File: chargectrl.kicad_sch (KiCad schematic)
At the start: 84 parts, among them Q2 SiRA00DP, Q3 SiRA00DP, Q4 SiRA00DP, Q5 SiRA00DP, U4 BQ25756RRVR, U5 TPS25730D, U6 MAX17614ATP+, U7 MAX17614ATP+

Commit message: Finalized V2
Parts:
- removed TP19, TP22: TEST POINT, symbol Connector:TestPoint
- C50, C51, C52, C53, C54, C55, C56, C57, C58, C59, C60, C61, C62, C63, C64, C65, C66, C67, C68, C69, C70, C71, C72, C73, C74, C75, C76, C77, C78, C79: footprint Capacitor_SMD:C_0402_1005Metric -> Capacitor_SMD:C_0402_1005Metric_Pad0.74x0.62mm_HandSolder
- D10, D11: footprint Diode_SMD:D_0402_1005Metric -> Diode_SMD:D_0402_1005Metric_Pad0.77x0.64mm_HandSolder
- R51: renamed from R49; footprint Resistor_SMD:R_0402_1005Metric -> Resistor_SMD:R_0402_1005Metric_Pad0.72x0.64mm_HandSolder
- R52: renamed from R50; footprint Resistor_SMD:R_0402_1005Metric -> Resistor_SMD:R_0402_1005Metric_Pad0.72x0.64mm_HandSolder
- R53: renamed from R51; footprint Resistor_SMD:R_0402_1005Metric -> Resistor_SMD:R_0402_1005Metric_Pad0.72x0.64mm_HandSolder
- R54: renamed from R52; footprint Resistor_SMD:R_0402_1005Metric -> Resistor_SMD:R_0402_1005Metric_Pad0.72x0.64mm_HandSolder
- R55: renamed from R53; footprint Resistor_SMD:R_0402_1005Metric -> Resistor_SMD:R_0402_1005Metric_Pad0.72x0.64mm_HandSolder
- R56: renamed from R54; footprint Resistor_SMD:R_0402_1005Metric -> Resistor_SMD:R_0402_1005Metric_Pad0.72x0.64mm_HandSolder
- R57: renamed from R55; footprint Resistor_SMD:R_0402_1005Metric -> Resistor_SMD:R_0402_1005Metric_Pad0.72x0.64mm_HandSolder
- R58: renamed from R56; footprint Resistor_SMD:R_0402_1005Metric -> Resistor_SMD:R_0402_1005Metric_Pad0.72x0.64mm_HandSolder
- R59: renamed from R57; footprint Resistor_SMD:R_0402_1005Metric -> Resistor_SMD:R_0402_1005Metric_Pad0.72x0.64mm_HandSolder
- R60: renamed from R58; footprint Resistor_SMD:R_0402_1005Metric -> Resistor_SMD:R_0402_1005Metric_Pad0.72x0.64mm_HandSolder
- R61: renamed from R59; footprint Resistor_SMD:R_0402_1005Metric -> Resistor_SMD:R_0402_1005Metric_Pad0.72x0.64mm_HandSolder
- R62: renamed from R60; footprint Resistor_SMD:R_0402_1005Metric -> Resistor_SMD:R_0402_1005Metric_Pad0.72x0.64mm_HandSolder
- R63: renamed from R61; footprint Resistor_SMD:R_0402_1005Metric -> Resistor_SMD:R_0402_1005Metric_Pad0.72x0.64mm_HandSolder
- R64: renamed from R62; footprint Resistor_SMD:R_0402_1005Metric -> Resistor_SMD:R_0402_1005Metric_Pad0.72x0.64mm_HandSolder
- R65: renamed from R63; footprint Resistor_SMD:R_0402_1005Metric -> Resistor_SMD:R_0402_1005Metric_Pad0.72x0.64mm_HandSolder
- R66: renamed from R64; footprint Resistor_SMD:R_0402_1005Metric -> Resistor_SMD:R_0402_1005Metric_Pad0.72x0.64mm_HandSolder
- R67: renamed from R65; footprint Resistor_SMD:R_0402_1005Metric -> Resistor_SMD:R_0402_1005Metric_Pad0.72x0.64mm_HandSolder
- R68: renamed from R66; footprint Resistor_SMD:R_0402_1005Metric -> Resistor_SMD:R_0402_1005Metric_Pad0.72x0.64mm_HandSolder
- R69: renamed from R67; footprint Resistor_SMD:R_0402_1005Metric -> Resistor_SMD:R_0402_1005Metric_Pad0.72x0.64mm_HandSolder
- R70: renamed from R68; footprint Resistor_SMD:R_0402_1005Metric -> Resistor_SMD:R_0402_1005Metric_Pad0.72x0.64mm_HandSolder
- R71: renamed from R69; footprint Resistor_SMD:R_0402_1005Metric -> Resistor_SMD:R_0402_1005Metric_Pad0.72x0.64mm_HandSolder
- R72: renamed from R70; footprint Resistor_SMD:R_0402_1005Metric -> Resistor_SMD:R_0402_1005Metric_Pad0.72x0.64mm_HandSolder
- R73: renamed from R71; footprint Resistor_SMD:R_0402_1005Metric -> Resistor_SMD:R_0402_1005Metric_Pad0.72x0.64mm_HandSolder
- R74: renamed from R72; footprint Resistor_SMD:R_0402_1005Metric -> Resistor_SMD:R_0402_1005Metric_Pad0.72x0.64mm_HandSolder
- R75: renamed from R73; footprint Resistor_SMD:R_0402_1005Metric -> Resistor_SMD:R_0402_1005Metric_Pad0.72x0.64mm_HandSolder
- R76: renamed from R74; footprint Resistor_SMD:R_0402_1005Metric -> Resistor_SMD:R_0402_1005Metric_Pad0.72x0.64mm_HandSolder
- R77: renamed from R75; footprint Resistor_SMD:R_0402_1005Metric -> Resistor_SMD:R_0402_1005Metric_Pad0.72x0.64mm_HandSolder
- R78: renamed from R76; footprint Resistor_SMD:R_0402_1005Metric -> Resistor_SMD:R_0402_1005Metric_Pad0.72x0.64mm_HandSolder
- R79: renamed from R77; footprint Resistor_SMD:R_0402_1005Metric -> Resistor_SMD:R_0402_1005Metric_Pad0.72x0.64mm_HandSolder
- R80: renamed from R78; footprint Resistor_SMD:R_0402_1005Metric -> Resistor_SMD:R_0402_1005Metric_Pad0.72x0.64mm_HandSolder
- R81: renamed from R79; footprint Resistor_SMD:R_0402_1005Metric -> Resistor_SMD:R_0402_1005Metric_Pad0.72x0.64mm_HandSolder
- R82: renamed from R80; footprint Resistor_SMD:R_0402_1005Metric -> Resistor_SMD:R_0402_1005Metric_Pad0.72x0.64mm_HandSolder
- R83: renamed from R81; footprint Resistor_SMD:R_0402_1005Metric -> Resistor_SMD:R_0402_1005Metric_Pad0.72x0.64mm_HandSolder
- R84: renamed from R82; footprint Resistor_SMD:R_0402_1005Metric -> Resistor_SMD:R_0402_1005Metric_Pad0.72x0.64mm_HandSolder
- R85: renamed from R83; footprint Resistor_SMD:R_0402_1005Metric -> Resistor_SMD:R_0402_1005Metric_Pad0.72x0.64mm_HandSolder
- R86: renamed from R84; footprint Resistor_SMD:R_0402_1005Metric -> Resistor_SMD:R_0402_1005Metric_Pad0.72x0.64mm_HandSolder
- R87: renamed from R85; footprint Resistor_SMD:R_0402_1005Metric -> Resistor_SMD:R_0402_1005Metric_Pad0.72x0.64mm_HandSolder
- R88: renamed from R86; footprint Resistor_SMD:R_0402_1005Metric -> Resistor_SMD:R_0402_1005Metric_Pad0.72x0.64mm_HandSolder
- R89: renamed from R87; footprint Resistor_SMD:R_0402_1005Metric -> Resistor_SMD:R_0402_1005Metric_Pad0.72x0.64mm_HandSolder
- TP19: renamed from TP20; footprint (none) -> TestPoint:TestPoint_Pad_1.0x1.0mm
- TP20: renamed from TP21; footprint (none) -> TestPoint:TestPoint_Pad_1.0x1.0mm
- renumbered U4 to U6, U5 to U7, U6 to U8, U7 to U9

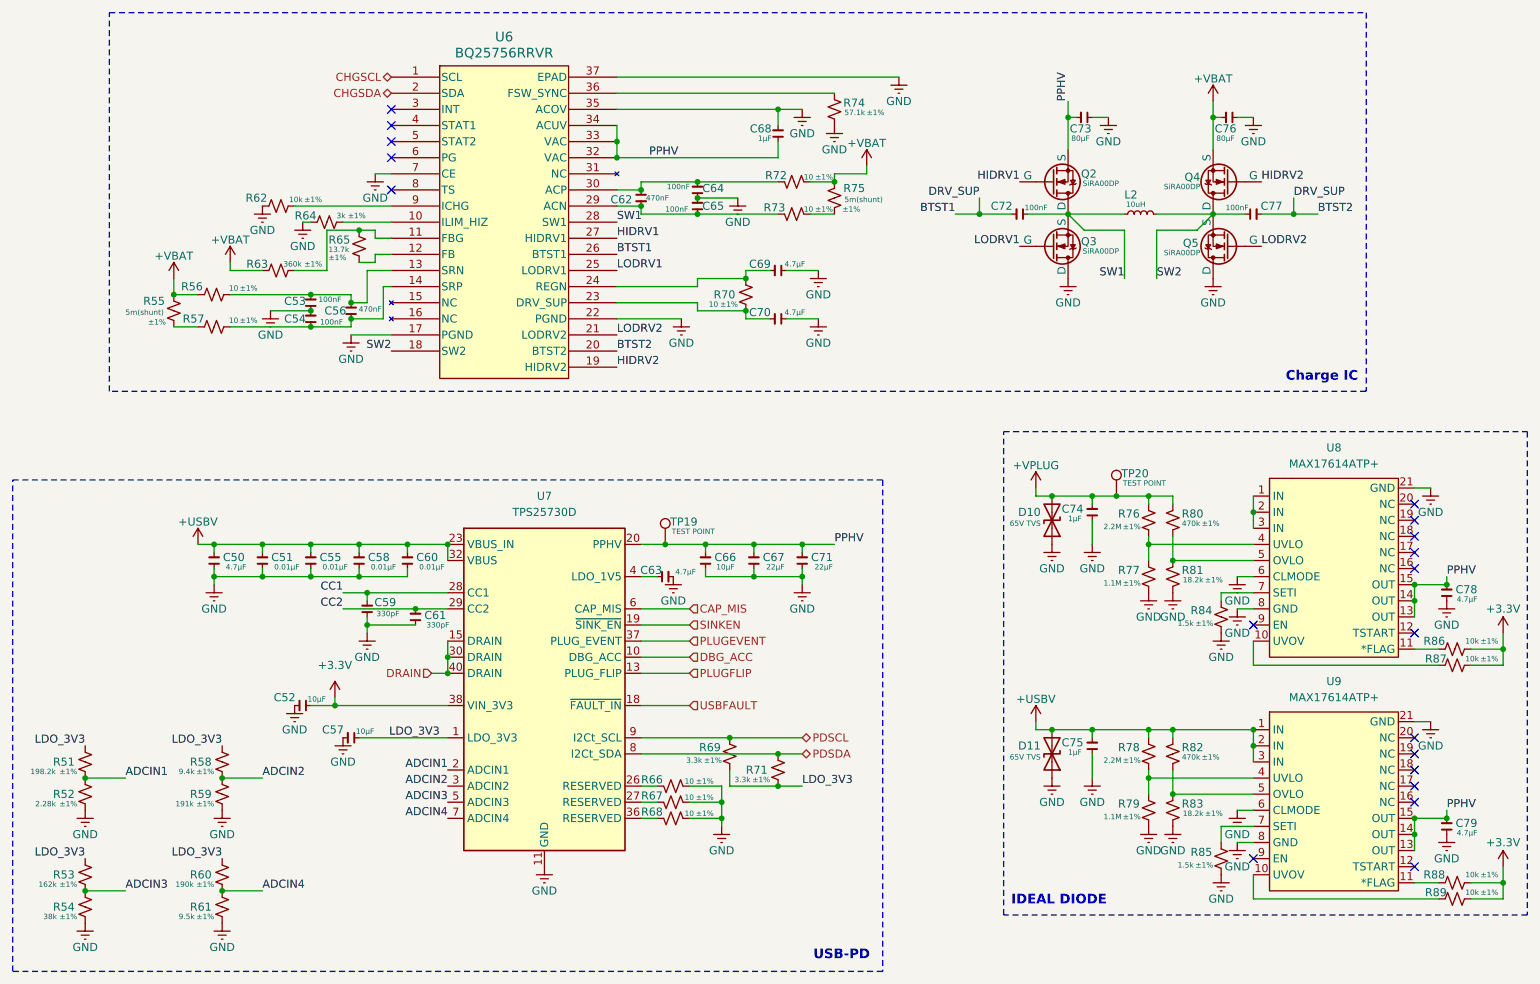
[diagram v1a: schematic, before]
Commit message: Fixed Ideal Diodes
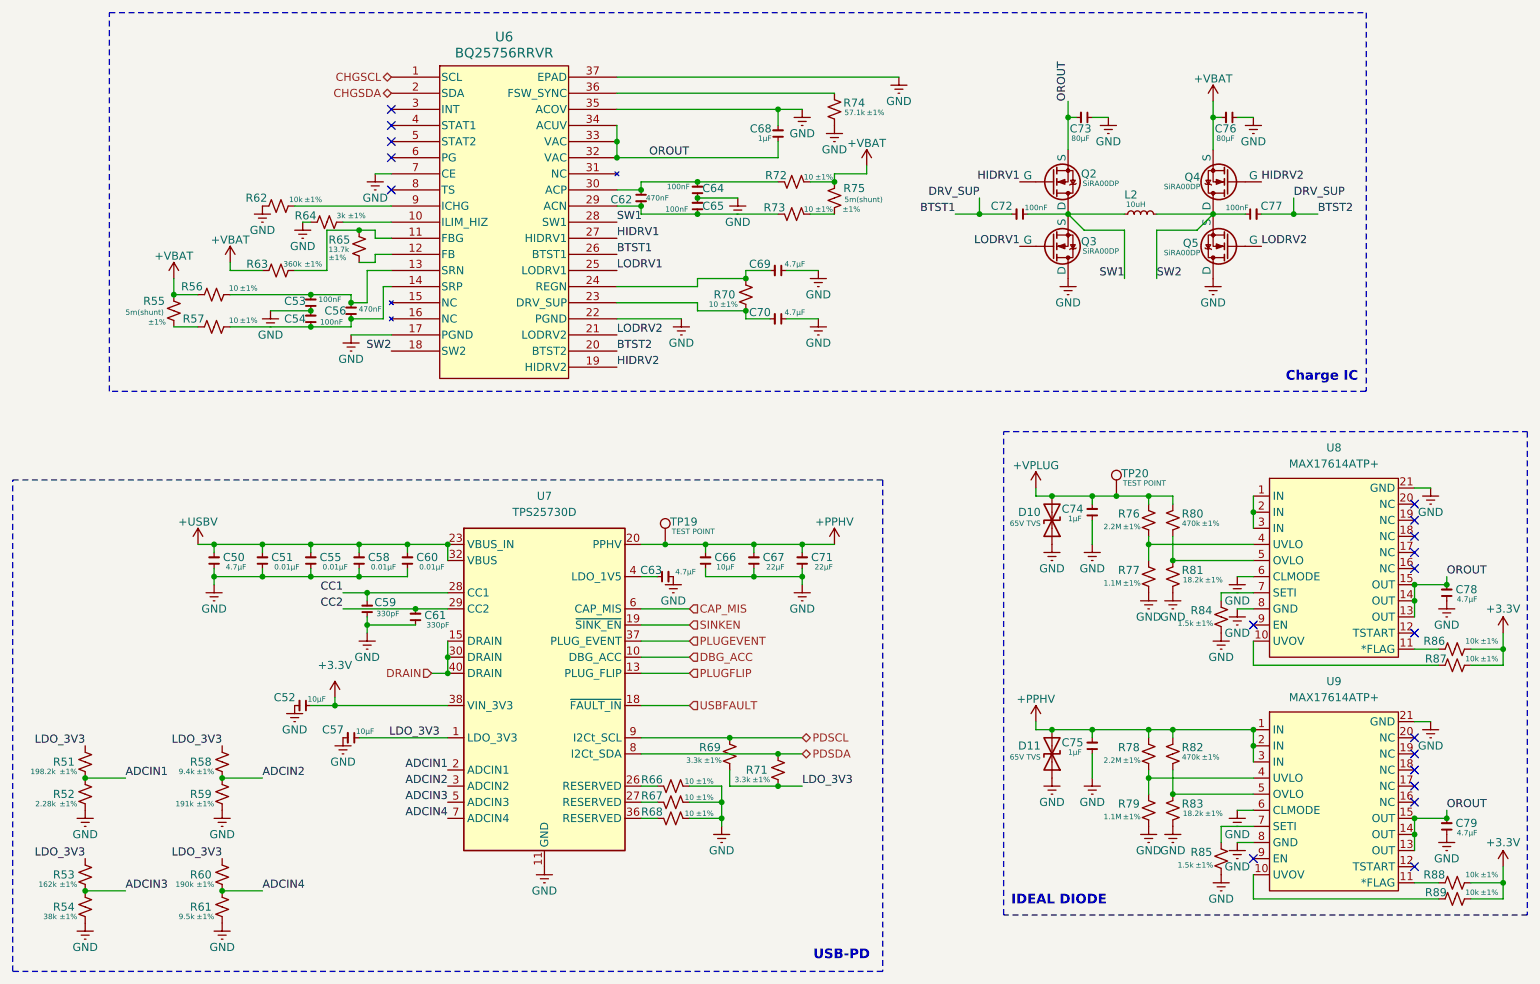
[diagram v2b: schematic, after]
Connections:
- net +USBV: no longer C75.2, D11.2 (A2), R78.1, R82.1, U9.1 (IN), U9.2 (IN), U9.3 (IN)
- net PPHV renamed OROUT
- net OROUT: no longer C66.2, C67.2, C71.2, TP19.1, U7.20 (PPHV)
- new net +PPHV: C66.2, C67.2, C71.2, C75.2, D11.2 (A2), R78.1, R82.1, TP19.1, U7.20 (PPHV), U9.1 (IN), U9.2 (IN), U9.3 (IN)
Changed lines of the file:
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@@
 		)
 	)
-	(label "PPHV"
+	(label "OROUT"
 		(at 118.11 44.45 0)
 		(effects
@@
 		)
 	)
-	(label "PPHV"
+	(label "OROUT"
 		(at 184.15 35.56 90)
 		(effects
@@
 		)
 	)
-	(label "PPHV"
+	(label "OROUT"
 		(at 243.84 147.32 0)
 		(effects
@@
 		)
 	)
-	(label "PPHV"
+	(label "OROUT"
 		(at 243.84 110.49 0)
 		(effects
@@
 		)
 	)
-	(label "PPHV"
-		(at 147.32 105.41 0)
-		(effects
-			(font
-				(size 1.27 1.27)
-				(thickness 0.1588)
-			)
-			(justify left bottom)
-		)
-	)
 	(label "DRV_SUP"
 		(at 170.18 50.8 180)
@@
 			)
 		)
-		(property "Value" "+USBV"
+		(property "Value" "+PPHV"
 			(at 179.07 129.794 0)
 			(effects
@@
 					(unit 1)
 				)
+			)
+		)
+	)
+	(symbol
+		(lib_id "power:+5V")
+		(at 147.32 105.41 0)
+		(unit 1)
+		(exclude_from_sim no)
+		(in_bom yes)
+		(on_board yes)
+		(dnp no)
+		(property "Reference" "#PWR0114"
+			(at 147.32 109.22 0)
+			(effects
+				(font
+					(size 1.27 1.27)
+				)
+				(hide yes)
+			)
+		)
+		(property "Value" "+PPHV"
+			(at 147.32 101.854 0)
+			(effects
+				(font
+					(size 1.27 1.27)
+				)
+			)
+		)
+		(property "Footprint" ""
+			(at 147.32 105.41 0)
+			(effects
+				(font
+					(size 1.27 1.27)
+				)
+				(hide yes)
+			)
+		)
+		(property "Datasheet" ""
+			(at 147.32 105.41 0)
+			(effects
+				(font
+					(size 1.27 1.27)
+				)
+				(hide yes)
+			)
+		)
+		(property "Description" "Power symbol creates a global label with name \"+5V\""
+			(at 147.32 105.41 0)
+			(effects
+				(font
+					(size 1.27 1.27)
+				)
+				(hide yes)
+			)
+		)
+		(pin "1"
+		)
+		(instances
+			(project "bms"
+				(path "/25bab91c-a0ce-4d39-aca4-3409cb6c9cc9/9fe912d2-630d-4776-83ae-5a5308a5b203"
+					(reference "#PWR0114")
+					(unit 1)
+				)

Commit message: EM-BMS1
good to order!
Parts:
- C50, C63, C69, C70, C78, C79: value 4.7µF -> 4.7uF
- C52, C57, C66: value 10µF -> 10uF
- C67, C71: value 22µF -> 22uF
- C73, C76: value 80µF -> 80uF
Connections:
- net DBG_ACC: no longer names the net of U7.10 (DBG_ACC)
- no-connect marks 19 -> 20
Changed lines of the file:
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@@
 	)
 	(no_connect
+		(at 116.84 123.19)
+	)
+	(no_connect
 		(at 238.76 140.97)
 	)
@@
 	(wire
 		(pts
-			(xy 124.46 123.19) (xy 116.84 123.19)
-		)
-		(stroke
-			(width 0)
-			(type default)
-		)
-	)
-	(wire
-		(pts
 			(xy 113.03 39.37) (xy 113.03 41.91)
 		)
@@
 		)
 	)
-	(hierarchical_label "DBG_ACC"
-		(shape input)
-		(at 124.46 123.19 0)
-		(effects
-			(font
-				(size 1.27 1.27)
-			)
-			(justify left)
-		)
-	)
 	(symbol
 		(lib_name "C_Small_1")
@@
 			)
 		)
-		(property "Value" "4.7µF"
+		(property "Value" "4.7uF"
 			(at 139.446 68.834 90)
 			(effects
@@
 			)
 		)
-		(property "Value" "4.7µF"
+		(property "Value" "4.7uF"
 			(at 125.476 109.728 90)
 			(effects
@@
 			)
 		)
-		(property "Value" "4.7µF"
+		(property "Value" "4.7uF"
 			(at 248.666 150.876 0)
 			(effects
@@
 			)
 		)
-		(property "Value" "22µF"
+		(property "Value" "22uF"
 			(at 147.066 108.966 0)
 			(effects
@@
 			)
 		)
-		(property "Value" "22µF"
+		(property "Value" "22uF"
 			(at 139.446 108.966 0)
 			(effects
@@
 			)
 		)
-		(property "Value" "4.7µF"
+		(property "Value" "4.7uF"
 			(at 54.61 108.966 0)
 			(effects
@@
 			)
 		)
-		(property "Value" "10µF"
+		(property "Value" "10uF"
 			(at 131.572 108.966 0)
 			(effects
@@
 			)
 		)
-		(property "Value" "4.7µF"
+		(property "Value" "4.7uF"
 			(at 248.666 114.046 0)
 			(effects
@@
 			)
 		)
-		(property "Value" "10µF"
+		(property "Value" "10uF"
 			(at 71.882 134.874 90)
 			(effects
@@
 			)
 		)
-		(property "Value" "4.7µF"
+		(property "Value" "4.7uF"
 			(at 139.446 61.214 90)
 			(effects
@@
 			)
 		)
-		(property "Value" "80µF"
+		(property "Value" "80uF"
 			(at 184.658 41.402 90)
 			(effects
@@
 			)
 		)
-		(property "Value" "10µF"
+		(property "Value" "10uF"
 			(at 64.262 129.794 90)
 			(effects
@@
 			)
 		)
-		(property "Value" "80µF"
+		(property "Value" "80uF"
 			(at 207.518 41.402 90)
 			(effects
